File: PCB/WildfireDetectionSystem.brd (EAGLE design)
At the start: 80 x 40 mm, 57 parts, among them IC1 STM32L476RGT6, J1 10118192-0001LF, J3 B4B-XH-A, J4 B5B-XH-A, SW1 1825910-6, U1 BME280, U2 LD39050PU33R, U3 NEO-6M-GPS, U4 24AA32A-I/MS, Y1 ABLS-8.000MHZ-B2-T, Y2 ECS-.327-12.5-12QS-TR

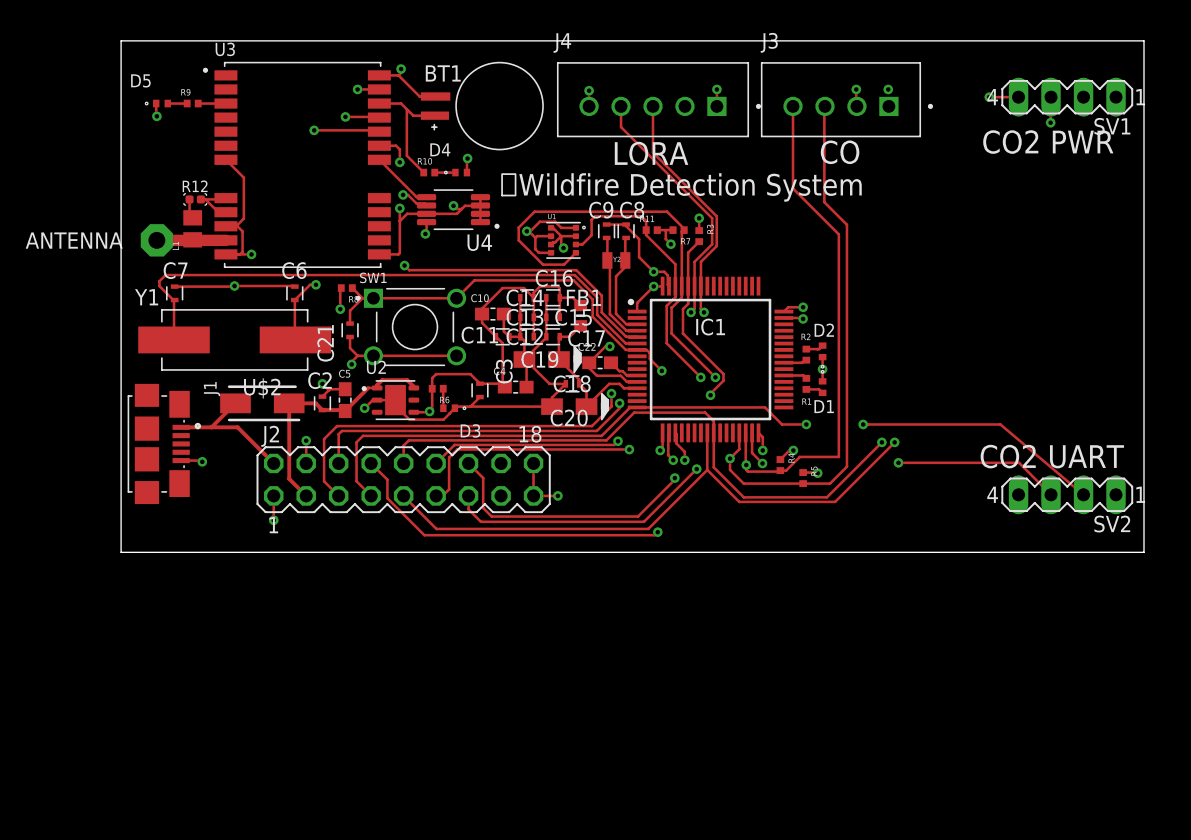
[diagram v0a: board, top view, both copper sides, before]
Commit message: edited board layout with comments from Kriteen
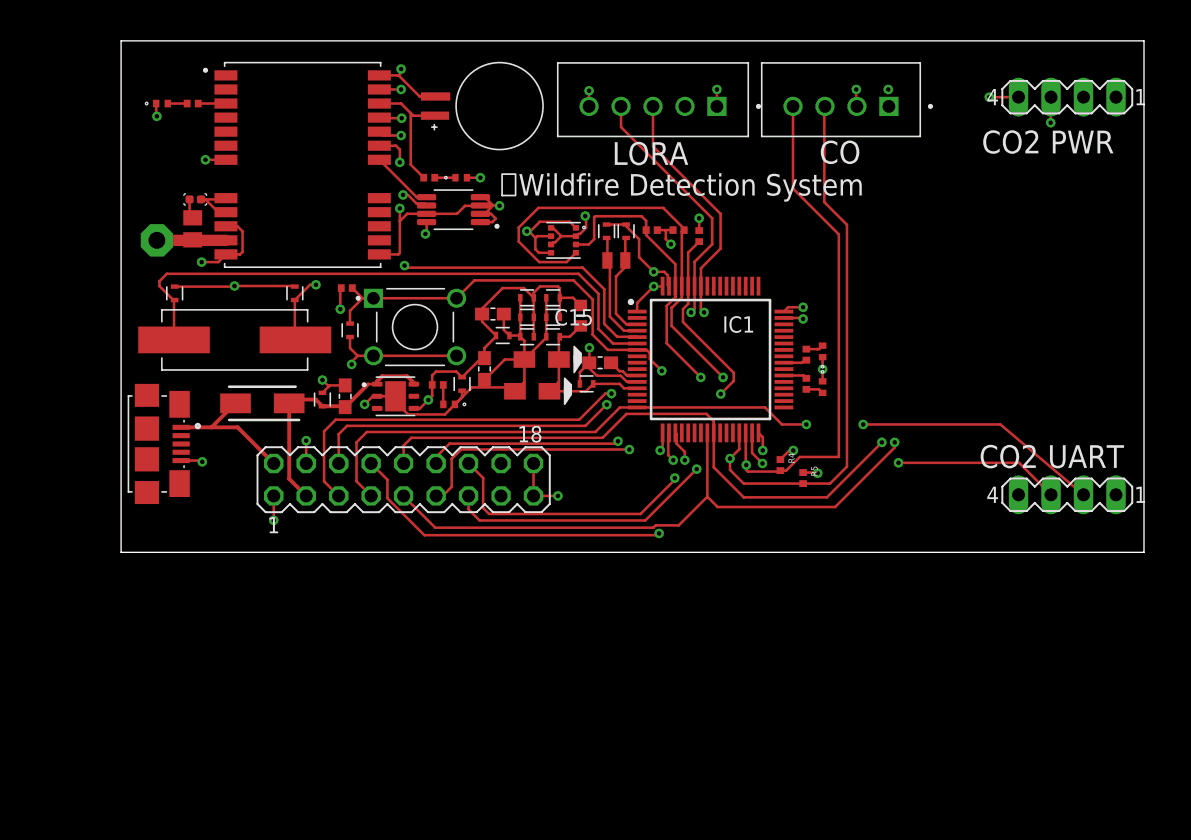
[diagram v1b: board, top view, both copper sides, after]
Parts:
- moved C20 3.14 mm to (32.2, 12.6)
- moved C4 2.82 mm to (28.4, 14.3), turned to 270 degrees
- moved C3 1.49 mm to (26.7, 13.2)
- moved C18 1.10 mm to (36.4, 13.2)
- moved D4 0.40 mm to (26.6, 29.3)
- moved R10 0.40 mm to (24.1, 29.3)
- moved C2 0.30 mm to (15.7, 12.0)
- moved C5 0.30 mm to (17.5, 12.2)
- moved D3 0.30 mm to (25.7, 11.6)
- moved U2 0.30 mm to (21.5, 12.2)
- moved R6 0.30 mm to (24.8, 13.1)
- moved C11 0.10 mm to (29.8, 17.0)
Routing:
- net UART3_TX_GPS: track 113.5 -> 106.5 mm
- net UART3_RX_GPS: track 106.0 -> 100.5 mm
- net GND: track 141.9 -> 138.2 mm, vias 23 -> 24
- net 3V3: track 62.5 -> 59.3 mm
- net PH1-OSC-OUT: track 47.3 -> 48.3 mm
- net BOOT0: track 34.6 -> 35.4 mm
- net PH0-OSC-IN: track 34.1 -> 34.9 mm
- net NRST: track 47.4 -> 48.2 mm
- net I2C1_SCL_BME: track 61.3 -> 62.1 mm
- net UART1_TX_LORA: track 60.5 -> 59.9 mm
- net VREF_PLUS: track 13.2 -> 13.8 mm
- net I2C1_SDA_BME: track 45.3 -> 45.9 mm

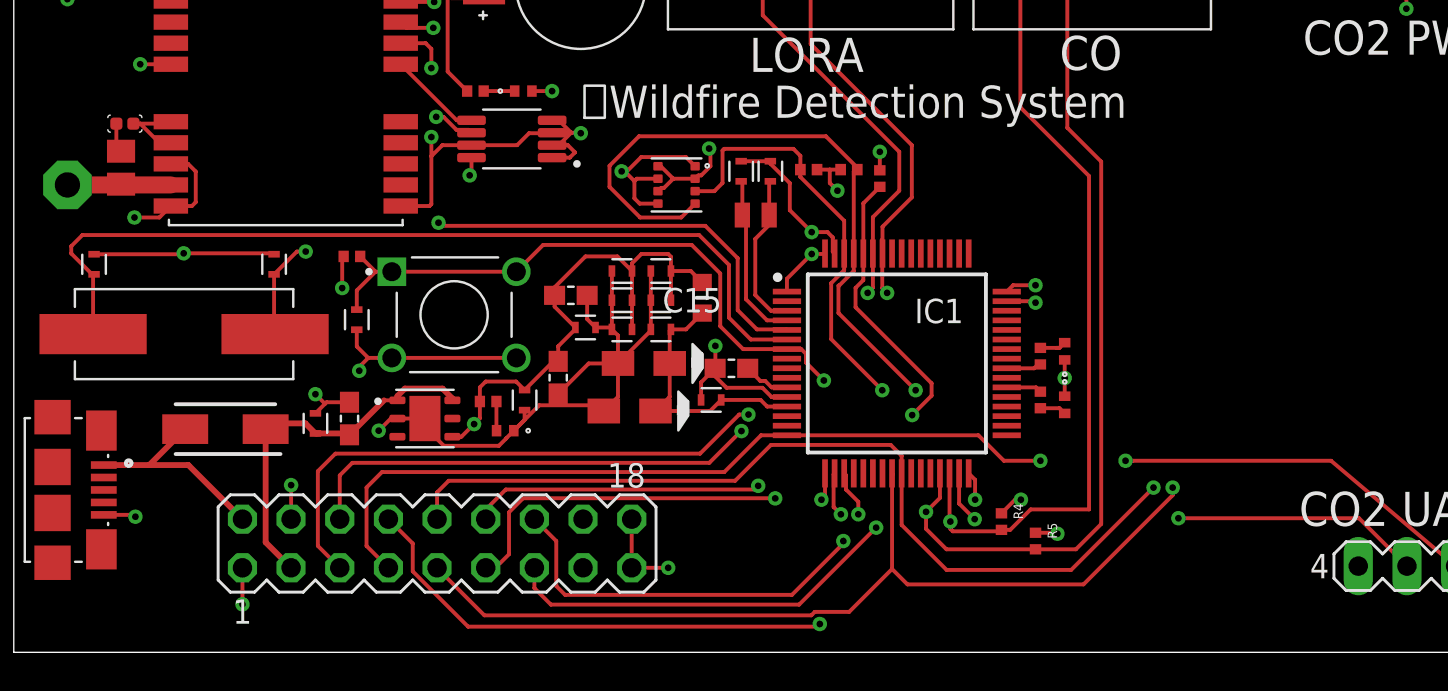
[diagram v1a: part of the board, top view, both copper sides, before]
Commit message: clearance set to .1mm
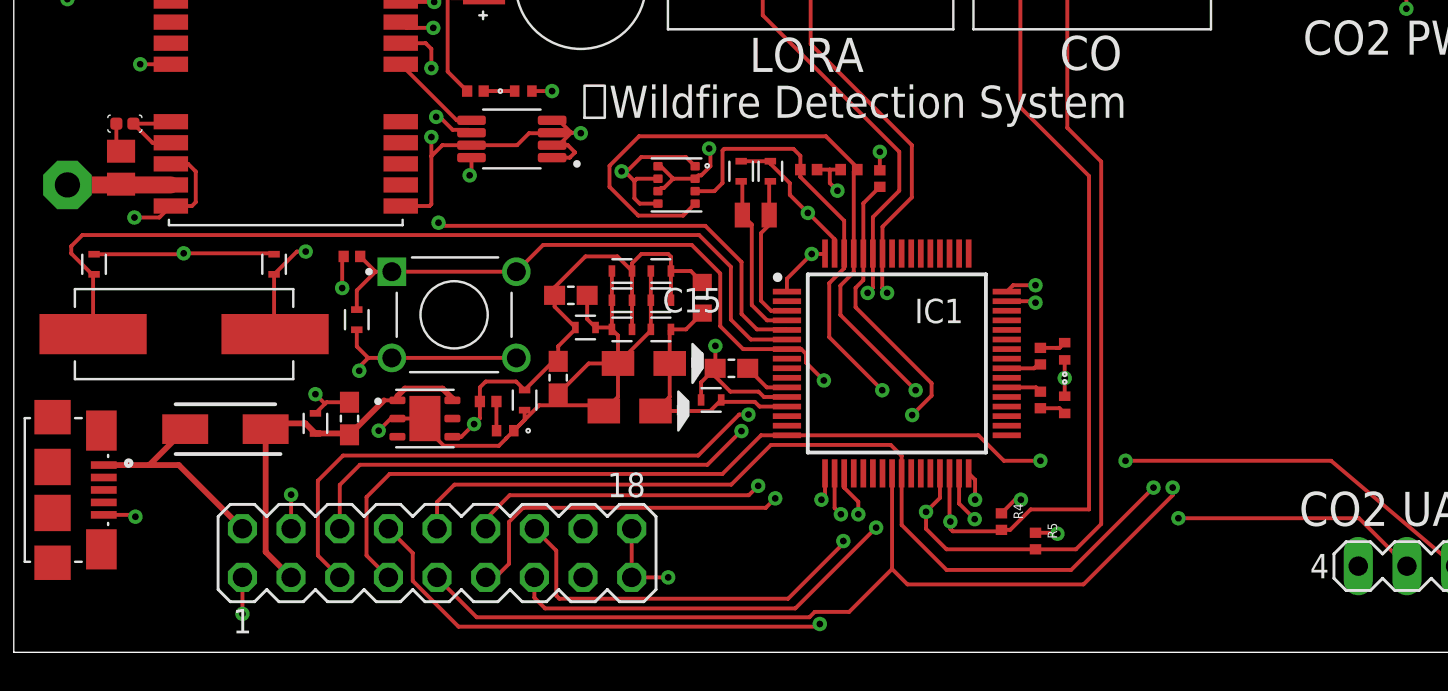
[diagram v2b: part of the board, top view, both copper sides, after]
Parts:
- moved J2 0.50 mm to (22.1, 5.18)
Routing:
- net GND: track 138.2 -> 137.4 mm
- net UART1_RX_LORA: track 56.6 -> 56.1 mm

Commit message: board and schematic changes
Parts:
- removed C15, C16, C17, C18: CC0402KRX7R7BB104, ce-capstone:CAPC1005X55N
- removed U4: 24AA32A-I/MS, 24AA32A-I_MS:SOP65P490X110-8N
- added C1, C23: CL05B104KO5NNNC, CL05B104KO5NNNC:CAPC1005X55N
- added C24, C25: CL10C200JB8NNNC, CL10C200JB8NNNC:CAPC1608X90N
- added U$1: 24LC32AT-I/SN, 24LC32AT-I_SN:SOIC127P794X203-8N
- C11, C12, C13, C14: value CC0402KRX7R7BB104 -> CL05B104KO5NNNC; device ce-capstone:CAPC1005X55N -> CL05B104KO5NNNC:CAPC1005X55N
- C2, C21: value CC0402KRX7R7BB104 -> CL10C200JB8NNNC; device ce-capstone:CAPC1005X55N -> CL10C200JB8NNNC:CAPC1608X90N
- C6, C7, C8, C9: value CC0402JRNPO9BN200 -> CL05B104KO5NNNC; device ce-capstone:CAPC1005X55N -> CL05B104KO5NNNC:CAPC1005X55N
- moved C7 30.6 mm to (34.8, 19.0), turned to 180 degrees
- moved C6 21.2 mm to (34.8, 20.3), turned to 180 degrees
- moved C21 11.9 mm to (6.40, 20.5), turned to 0 degrees
- moved C2 9.01 mm to (12.9, 20.5), turned to 180 degrees
- moved C8 8.78 mm to (34.8, 17.7), turned to 180 degrees
- moved C14 8.76 mm to (36.1, 12.3), turned to 90 degrees
- moved C13 8.30 mm to (37.4, 12.3), turned to 90 degrees
- moved C9 7.28 mm to (32.7, 20.1), turned to 180 degrees
- moved C11 3.40 mm to (32.7, 18.8), turned to 180 degrees
- moved D1 1.20 mm to (56.1, 12.9)
- moved D2 1.20 mm to (56.1, 15.7)
- moved IC1 1.20 mm to (47.3, 15.1)
- moved R11 1.20 mm to (42.7, 25.2)
- moved R4 1.20 mm to (52.8, 6.83)
- moved Y2 1.20 mm to (39.9, 22.8)
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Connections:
- net 3V3: now also C6.1, C7.1, C8.1, C9.1, U$1.8; no longer C13.1, C14.1, C15.1, C16.1, U4.8
- net 5V: now also C23.1; no longer C2.1
- net GND: now also C1.2, C21.2, C23.2, C24.2, C25.2, U$1.1, U$1.2, U$1.3, U$1.4, U$1.7; no longer C15.2, C16.2, C17.2, C18.2, C21.1, U4.1, U4.2, U4.3, U4.4, U4.7
- net GPS_SCL: now also U$1.6; no longer U4.6
- net GPS_SDA: now also U$1.5; no longer U4.5
- net NRST: now also C1.1; no longer C21.2
- net PC14-OSC32-IN: now also C24.1; no longer C8.1
- net PC15-OSC32-OUT: now also C25.1; no longer C9.1
- net PH0-OSC-IN: now also C2.1; no longer C6.1
- net PH1-OSC-OUT: now also C21.1; no longer C7.1
- net VREF_PLUS: now also C13.1, C14.1; no longer C17.1, C18.1
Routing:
- net GND: track 137.4 -> 127.8 mm, vias 24 -> 25
- net I2C1_SDA_BME: track 46.2 -> 51.7 mm
- net I2C1_SCL_BME: track 62.1 -> 65.8 mm
- net PH1-OSC-OUT: track 47.9 -> 45.0 mm
- net VREF_PLUS: track 13.8 -> 16.5 mm
- net NRST: track 48.2 -> 50.6 mm
- net UART3_RX_GPS: track 100.7 -> 103.1 mm
- net UART3_TX_GPS: track 106.3 -> 108.7 mm
- net I2C2_SDA_CO: track 65.9 -> 67.6 mm
- net I2C2_SCL_CO: track 66.1 -> 67.8 mm
- net UART1_TX_LORA: track 60.1 -> 61.8 mm
- net UART1_RX_LORA: track 56.1 -> 57.7 mm
- net PH0-OSC-IN: track 34.9 -> 36.5 mm
- net N$6: track 2.46 -> 3.66 mm
- net BOOT0: track 35.2 -> 36.4 mm
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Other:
- board text added: "3v3"

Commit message: pcb v2
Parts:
- removed ANTENNA: (no value), discrete:PAD-01
- added BATTERY: (no value), con-lstb:MA03-1
- added C15, C17: 4.7uF, rcl:C0603
- added C16, C30: 1uF, rcl:C0603
- added C18, C26, C27, C28, C33, C34, C36: 22uF, rcl:C0603
- added C29: .1uF, rcl:C0603
- added C31: 220nF, rcl:C0603
- added C32, C35, C37: 10uF, rcl:C0603
- added C38: 3.3nF, rcl:C0603
- added D6: SML-P12MTT86, ce-capstone:LED_SML-P11UTT86R
- added D7: SML-P12VTT86, ce-capstone:LED_SML-P11UTT86R
- added J7: B4B-PH-K-S, B4B-PH-K-S:JST_B4B-PH-K-S
- added J8: U.FL-R-SMT-1(10), U.FL-R-SMT-1_10_:HRS_U.FL-R-SMT-1(10)
- added J9: B2B-PH-K-S, B2B-PH-K-S:JST_B2B-PH-K-S
- added L2: 8uH, rcl:L3225M
- added L3: 1uH, rcl:L3225M
- added L4: 2.2uH, rcl:L3225M
- added R13: 1.18k, rcl:R0603
- added R14: 1.13k, rcl:R0603
- added R15, R16: 1k, rcl:R0603
- added R17, R18, R21, R22: 100k, rcl:R0603
- added R19: 24.9k, rcl:R0603
- added R20: 732k, rcl:R0603
- added STLINK_INTERFACE: (no value), con-lstb:MA03-2
- added U4: TPS62142RGTT, TPS62142RGTT:QFN50P300X300X100-17N
- added U5: TPS61022RWUR, TPS61022RWUR:CONV_TPS61022RWUR
- added U6: LMR33630ADDA, LMR33630ADDA:VREG_LM5017MR/NOPB
- added U7: BQ24074RGTR, BQ24074RGTR:QFN50P300X300X100-17N
- turned SV2 to 0 degrees
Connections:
- new net BAT: BATTERY.1, C15.1, U7.2, U7.3
- new net BOOT: C29.2, U6.7
- new net CHG: D6.C, U7.9
- new net FB: R17.2, R19.1, U6.5
- new net FB2: R20.2, R21.1, U5.4
- new net ILIM: R13.2, U7.12
- new net ISET: R14.2, U7.16
- new net N$17: D6.A, R16.1
- new net N$18: D7.A, R15.1
- new net N$28: U7.15
- new net PG: R22.1, U4.4
- new net PG2: R18.1, U6.4
- new net PGOOD: D7.C, U7.7
- new net SOLAR_IN: C31.1, C32.1, J9.2, U6.2, U6.3
- new net SS/TR: C38.1, U4.9
- new net SW: L4.1, U4.1, U4.2, U4.3
- new net SW2: L3.1, U5.2
- new net SW3: C29.1, L2.2, U6.8
- new net SWCLK: IC1.49, STLINK_INTERFACE.4
- new net SWDIO: IC1.46, STLINK_INTERFACE.6
- new net SYS: C17.1, C35.1, C37.1, L3.2, R15.2, R16.2, U4.10, U4.11, U4.12, U4.13, U5.5, U5.7, U7.10, U7.11, U7.5
- new net TRACESWO: IC1.55, STLINK_INTERFACE.2
- new net TS: BATTERY.3, U7.1
- new net VCC: C30.1, R18.2, U6.6
- net 3V3: now also C36.1, J7.1, L4.2, R22.2, STLINK_INTERFACE.5, U4.14; no longer SV1.4
- net 5V: now also C33.1, C34.1, R20.1, SV1.4, U5.3
- net 5V_IN: now also C16.1, C18.1, C26.1, C27.1, C28.1, L2.1, R17.1, U7.13
- net GND: now also BATTERY.2, C15.2, C16.2, C17.2, C18.2, C26.2, C27.2, C28.2, C30.2, C31.2, C32.2, C33.2, C34.2, C35.2, C36.2, C37.2, C38.2, J7.4, J8.1, J8.3, J9.1, R13.1, R14.1, R19.2, R21.2, STLINK_INTERFACE.1, U4.15, U4.16, U4.17, U4.5, U4.6, U4.7, U4.8, U5.1, U5.6, U6.1, U6.9, U7.14, U7.17, U7.4, U7.6, U7.8
- net NRST: now also STLINK_INTERFACE.3
- net RF_IN: now also J8.2; no longer ANTENNA.1
- net UART1_RX_LORA: now also J4.4; no longer J4.3
- net UART1_TX_LORA: now also J4.3; no longer J4.4
- net UART3_RX_GPS: now also J7.3
- net UART3_TX_GPS: now also J7.2
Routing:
- net 5V: track 19.9 -> 136.5 mm
- net GND: track 127.8 -> 203.1 mm, vias 25 -> 44
- net 5V_IN: track 11.3 -> 72.1 mm
- net SYS: track 0.00 -> 49.1 mm
- net NRST: track 50.6 -> 73.9 mm
- net SWDIO: track 0.00 -> 16.6 mm
- net 3V3: track 59.3 -> 74.5 mm, vias 18 -> 20
- net UART3_RX_GPS: track 103.1 -> 116.1 mm, vias 2 -> 4
- net SW2: track 0.00 -> 10.6 mm, vias 0 -> 2
- net SOLAR_IN: track 0.00 -> 10.4 mm
- net TRACESWO: track 0.00 -> 9.95 mm
- net SWCLK: track 0.00 -> 9.76 mm
- net FB: track 0.00 -> 6.99 mm, vias 0 -> 2
- net SW3: track 0.00 -> 6.70 mm
- net BAT: track 0.00 -> 6.63 mm
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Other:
- board size 80 x 40 mm -> 80 x 60 mm
- board text added: "Battery"
- board text added: "Ember Watch"
- board text added: "Solar"
- board text added: "⣿⣿⣿⣿⣿⣿⣿⣿⣿⣿⣿⣿⣿⣿⣿⣿⣿⣿⣿⣿⣿⣿⣿⣿⣿⣿⣿⣿⣿⣿ ⣿⣿⣿⣿⣿⣿⣿⣿⡿⠿⣿⣿⣿⣿⣿⣿⣿⡎⠻⣿⣿⣿⣿⣿⣿⣿⣿⣿⣿⣿ ⣿⣿⣿⣿⣿⣿⣿⣿⡇⠀⢻⣿⣿⢿⣿⣿⣿⡇⠀⠈⢻⣿⣿⣿⣿⣿⣿⣿⣿⣿ ⣿⣿⣿⣿⣿⣿⣿⣿⣷⡀⣸⣿⣿⠈⠙⠛⠋⠀⠀⠀⠈⣿⣿⣿⣿⣿⣿⣿⣿⣿ ⣿⣿⣿⣿⣿⣿⣿⣿⢿⣿⣿⣿⣿⠀⠀⠀⠀⠀⠀⠀⢀⣿⣿⣿⣿⣿⣿⣿⣿⣿ ⣿⣿⣿⣿⣿⣿⡟⠁⠈⢿⣿⣿⠇⠀⠀⠀⠀⠀⠀⠀⣼⣿⣿⣿⣿⣿⣿⣿⣿⣿ ⣿⣿⣿⣿⣿⡏⠀⠀⠀⠀⠈⠀⠀⠀⢠⡀⣀⣴⠀⠀⣿⣿⣿⣿⣏⠻⣿⣿⣿⣿ ⣿⣿⣿⣿⣿⠁⠀⠀⠀⠀⠀⠀⠀⠀⣼⣿⣿⣿⠀⠀⠙⢿⣿⣿⡿⠀⠘⣿⣿⣿ ⣿⣿⣿⣿⣿⡆⠀⠀⠀⣦⣄⣠⣴⣾⣿⣿⣿⣿⡀⠀⠀⠀⠉⠉⠀⠀⠀⣿⣿⣿ ⣿⣿⣿⣿⣿⣷⠀⠀⠀⢹⣿⣿⡿⠟⢛⣿⣿⣿⣷⣄⠀⢀⠀⠀⠀⠀⢠⣿⣿⣿ ⣿⣿⣿⣿⣿⣿⣧⣠⣴⠾⠛⢁⡠⠖⠋⠉⠹⣿⣿⣿⣿⡟⠀⠀⠀⣠⣿⣿⣿⣿ ⣿⣿⣿⣿⣿⡿⠟⠋⠀⠀⠀⠀⣠⡶⠾⠿⠶⣿⡆⠉⠉⠛⠻⠷⢾⣿⣿⣿⣿⣿ ⣿⣿⣿⣿⡇⠀⠀⠀⠀⡀⠀⣸⡏⢠⠔⠙⣦⡈⢿⠀⠀⠐⠲⠤⣤⣴⣿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"
- board text removed: "🔥Wildfire Detection System"

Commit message: pcbv2
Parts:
- removed C23: CL05B104KO5NNNC, CL05B104KO5NNNC:CAPC1005X55N
- removed C3: CC0402KRX7R7BB104, ce-capstone:CAPC1005X55N
- removed C4, C5: CC0603KRX5R7BB105, ce-capstone:CAPC1608X90
- removed D3: SML-P12MTT86, ce-capstone:LED_SML-P11UTT86R
- removed R6: RC0402FR-071KL, ce-capstone:RESC1005X40N
- removed U$2: STPS1L30A, ce-capstone:DIOM5226X223N
- removed U2: LD39050PU33R, ce-capstone:SON95P300X300X100-7N
- added D10, D8, D9: SS34LWH, SS34LWH:SODFL3718X102N
- added R23: 10k, rcl:R0603
- BT1: value MS621FE-FL11E -> 1056TR; device MS621FE-FL11E:BAT_MS621FE-FL11E -> 1056TR:BAT_1056TR
- SW1: value 1825910-6 -> 434133025816; device ce-capstone:SW_1825910-6-4 -> 434133025816:434133025816
- moved J3 47.2 mm to (49.1, -11.2)
- moved BT1 27.5 mm to (56.8, 30.6), turned to 0 degrees
- moved STLINK_INTERFACE 15.1 mm to (61.1, 15.8), turned to 270 degrees
- moved J4 9.00 mm to (32.6, 35.4)
- moved R4 4.97 mm to (54.2, 2.06), turned to 0 degrees
- moved R5 4.52 mm to (52.0, 2.06), turned to 180 degrees
- moved C1 3.18 mm to (20.1, 19.7)
- moved SW1 1.98 mm to (24.3, 19.1)
- moved R3 1.41 mm to (45.4, 25.7)
- moved R7 1.21 mm to (43.7, 24.7)
- moved C31 1.10 mm to (7.50, -3.60)
- moved C32 1.10 mm to (9.70, -3.60)
- moved C28 0.90 mm to (34.2, -5.60)
- moved C18 0.90 mm to (27.6, -5.60)
- moved C26 0.90 mm to (29.8, -5.60)
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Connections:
- removed net N$1: D3.A, R6.1
- new net 5V_IN_SOLAR: C18.1, C26.1, C27.1, C28.1, D9.A, L2.1, R17.1
- new net 5V_IN_USB: D10.A, J1.1
- new net N$15: D8.C, U6.2, U6.3
- net 3V3: no longer C3.1, C4.1, R6.2, U2.4
- net 5V: no longer C23.1, C5.1, U$2.1, U2.1, U2.6
- net 5V_IN: now also D10.C, D9.C, R16.2; no longer C18.1, C26.1, C27.1, C28.1, J1.1, L2.1, R17.1, U$2.2
- net GND: now also BT1.N, R23.1; no longer BT1.-, C23.2, C3.2, C4.2, C5.2, D3.C, U2.2, U2.7
- net N$10: now also BT1.P; no longer BT1.+
- net SOLAR_IN: now also D8.A; no longer U6.2, U6.3
- net SYS: no longer R16.2
- net TS: now also R23.2; no longer BATTERY.3
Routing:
- net N$10: track 10.2 -> 34.7 mm, vias 0 -> 2
- net I2C2_SCL_CO: track 68.9 -> 49.6 mm, vias 2 -> 4
- net 5V_IN_SOLAR: track 0.00 -> 17.9 mm
- net 5V: track 136.5 -> 119.3 mm
- net I2C2_SDA_CO: track 68.5 -> 55.4 mm, vias 2 -> 4
- net 3V3: track 74.5 -> 64.1 mm, vias 20 -> 19
- net TRACESWO: track 9.95 -> 19.1 mm
- net UART1_RX_LORA: track 60.7 -> 68.1 mm
- net 5V_IN: track 72.1 -> 64.7 mm, vias 0 -> 3
- net UART1_TX_LORA: track 61.8 -> 68.8 mm
- net GND: track 203.1 -> 196.7 mm, vias 44 -> 53
- net SWDIO: track 16.6 -> 11.3 mm
- net N$15: track 0.00 -> 4.17 mm
- net 5V_IN_USB: track 0.00 -> 4.00 mm
- net SWCLK: track 9.76 -> 13.6 mm
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- added copper zone on layer 15, net 3V3
- removed copper zone on layer 3, net 3V3
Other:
- board text added: ") ( ( ) ) ) ) ( ( ) ) ( )( )( ) ) ( ( ) ) ) ) ) ( ( ) ( ) ) ( ( ) )( )( ( ) ) ( { ) ( ) ) ( (} ( ) { ( ) { ) ( } ) ) { } ) { ( ) } ( ( ) { } ) { ()"
- board text added: "+"
- board text added: "Created by: Kevin Yu Jake Gilbert Manny Lemus Frank Xiao Aliston Ma"
- board text added: "GPS"
- board text removed: "⣿⣿⣿⣿⣿⣿⣿⣿⣿⣿⣿⣿⣿⣿⣿⣿⣿⣿⣿⣿⣿⣿⣿⣿⣿⣿⣿⣿⣿⣿ ⣿⣿⣿⣿⣿⣿⣿⣿⡿⠿⣿⣿⣿⣿⣿⣿⣿⡎⠻⣿⣿⣿⣿⣿⣿⣿⣿⣿⣿⣿ ⣿⣿⣿⣿⣿⣿⣿⣿⡇⠀⢻⣿⣿⢿⣿⣿⣿⡇⠀⠈⢻⣿⣿⣿⣿⣿⣿⣿⣿⣿ ⣿⣿⣿⣿⣿⣿⣿⣿⣷⡀⣸⣿⣿⠈⠙⠛⠋⠀⠀⠀⠈⣿⣿⣿⣿⣿⣿⣿⣿⣿ ⣿⣿⣿⣿⣿⣿⣿⣿⢿⣿⣿⣿⣿⠀⠀⠀⠀⠀⠀⠀⢀⣿⣿⣿⣿⣿⣿⣿⣿⣿ ⣿⣿⣿⣿⣿⣿⡟⠁⠈⢿⣿⣿⠇⠀⠀⠀⠀⠀⠀⠀⣼⣿⣿⣿⣿⣿⣿⣿⣿⣿ ⣿⣿⣿⣿⣿⡏⠀⠀⠀⠀⠈⠀⠀⠀⢠⡀⣀⣴⠀⠀⣿⣿⣿⣿⣏⠻⣿⣿⣿⣿ ⣿⣿⣿⣿⣿⠁⠀⠀⠀⠀⠀⠀⠀⠀⣼⣿⣿⣿⠀⠀⠙⢿⣿⣿⡿⠀⠘⣿⣿⣿ ⣿⣿⣿⣿⣿⡆⠀⠀⠀⣦⣄⣠⣴⣾⣿⣿⣿⣿⡀⠀⠀⠀⠉⠉⠀⠀⠀⣿⣿⣿ ⣿⣿⣿⣿⣿⣷⠀⠀⠀⢹⣿⣿⡿⠟⢛⣿⣿⣿⣷⣄⠀⢀⠀⠀⠀⠀⢠⣿⣿⣿ ⣿⣿⣿⣿⣿⣿⣧⣠⣴⠾⠛⢁⡠⠖⠋⠉⠹⣿⣿⣿⣿⡟⠀⠀⠀⣠⣿⣿⣿⣿ ⣿⣿⣿⣿⣿⡿⠟⠋⠀⠀⠀⠀⣠⡶⠾⠿⠶⣿⡆⠉⠉⠛⠻⠷⢾⣿⣿⣿⣿⣿ ⣿⣿⣿⣿⡇⠀⠀⠀⠀⡀⠀⣸⡏⢠⠔⠙⣦⡈⢿⠀⠀⠐⠲⠤⣤⣴⣿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"

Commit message: pcbv2
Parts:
- removed L2: 8uH, rcl:L3225M
- added C3: 22uF, JLC PCB Basic Parts_loc:C0603
- added L5: L_4R7_0603, JLC PCB Basic Parts_loc:R0603
- added L6: L_2R2_0805, JLC PCB Basic Parts_loc:R0805
- C15, C16, C17, C18, C26, C27, C28, C29, C30, C31, C32, C33, C34, C35, C36, C37, C38: device rcl:C0603 -> JLC PCB Basic Parts_loc:C0603
- L3, L4: device rcl:L3225M -> JLC PCB Basic Parts_loc:R0805
- R15, R16, R17, R18, R21, R22, R23: device rcl:R0603 -> JLC PCB Basic Parts_loc:R0603
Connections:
- new net N$1: L5.2, L6.1
- net 5V: now also C3.1
- net 5V_IN_SOLAR: now also L5.1; no longer L2.1
- net GND: now also C3.2
- net SW3: now also L6.2; no longer L2.2
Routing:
- net 5V: track 119.3 -> 121.6 mm
- net GND: track 196.7 -> 199.0 mm
- net N$1: track 0.00 -> 2.24 mm
- net SW3: track 6.70 -> 8.47 mm
- net I2C1_SDA_BME: track 51.7 -> 51.0 mm, vias 3 -> 2
- net SYS: track 49.9 -> 50.4 mm
